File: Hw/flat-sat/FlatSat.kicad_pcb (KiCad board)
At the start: 4 copper layers, 0 parts

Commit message: fet(Hw):Init_floorplan_Update_LCSC#
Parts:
- added C1: 0.1uF, Capacitor_SMD:C_0402_1005Metric, F.Cu at (175.7, 70.3)
- added C10: 1nF, Capacitor_SMD:C_0402_1005Metric, F.Cu at (120.3, 85.0)
- added C11: 470nF, Capacitor_SMD:C_0402_1005Metric, F.Cu at (116.7, 79.4)
- added C12: 1nF, Capacitor_SMD:C_0402_1005Metric, F.Cu at (120.4, 89.4)
- added C13: 0.1uF, Capacitor_SMD:C_0402_1005Metric, F.Cu at (175.7, 80.2)
- added C14: 0.1uF, Capacitor_SMD:C_0402_1005Metric, F.Cu at (178.6, 70.3)
- added C15: 100pF, Capacitor_SMD:C_0402_1005Metric, F.Cu at (161.4, 70.6)
- added C16: 3.3pF, Capacitor_SMD:C_0402_1005Metric, F.Cu at (161.4, 73.1)
- added C17: 3.3pF, Capacitor_SMD:C_0402_1005Metric, F.Cu at (161.4, 75.6)
- added C18: 0.1uF, Capacitor_SMD:C_0402_1005Metric, F.Cu at (178.6, 72.3)
- added C19: 0.1uF, Capacitor_SMD:C_0402_1005Metric, F.Cu at (178.6, 74.3)
- added C2: 100pF, Capacitor_SMD:C_0402_1005Metric, F.Cu at (123.6, 87.2)
- added C20: 47pF, Capacitor_SMD:C_0402_1005Metric, F.Cu at (161.4, 78.1)
- added C21: 1nF, Capacitor_SMD:C_0402_1005Metric, F.Cu at (161.4, 80.6)
- added C22: 470nF, Capacitor_SMD:C_0402_1005Metric, F.Cu at (161.4, 83.2)
- added C23: 1nF, Capacitor_SMD:C_0402_1005Metric, F.Cu at (161.4, 85.7)
- added C24: 0.1uF, Capacitor_SMD:C_0402_1005Metric, F.Cu at (110.8, 81.0)
- added C25: 0.1uF, Capacitor_SMD:C_0402_1005Metric, F.Cu at (109.9, 81.0)
- added C26: 1uF, Capacitor_SMD:C_0402_1005Metric, F.Cu at (111.7, 93.1)
- added C27: 0.1uF, Capacitor_SMD:C_0402_1005Metric, F.Cu at (109.0, 81.0)
- added C28: 0.1uF, Capacitor_SMD:C_0402_1005Metric, F.Cu at (106.2, 81.0)
- added C29: 27pF, Capacitor_SMD:C_0402_1005Metric, F.Cu at (103.6, 94.6)
- added C3: 3.3pF, Capacitor_SMD:C_0402_1005Metric, F.Cu at (125.0, 82.7)
- added C30: 27pF, Capacitor_SMD:C_0402_1005Metric, F.Cu at (108.9, 93.2)
- added C31: 1uF, Capacitor_SMD:C_0402_1005Metric, F.Cu at (114.2, 83.8)
- added C32: 0.1uF, Capacitor_SMD:C_0402_1005Metric, F.Cu at (101.0, 84.6)
- added C33: 0.1uF, Capacitor_SMD:C_0402_1005Metric, F.Cu at (114.2, 84.7)
- added C34: 0.1uF, Capacitor_SMD:C_0402_1005Metric, F.Cu at (114.2, 88.7)
- added C35: 0.1uF, Capacitor_SMD:C_0402_1005Metric, F.Cu at (110.8, 93.1)
- added C36: 0.1uF, Capacitor_SMD:C_0402_1005Metric, F.Cu at (100.8, 88.3)
- added C37: 0.1uF, Capacitor_SMD:C_0402_1005Metric, F.Cu at (184.3, 78.2)
- added C4: 3.3pF, Capacitor_SMD:C_0402_1005Metric, F.Cu at (123.5, 88.7)
- added C5: 0.1uF, Capacitor_SMD:C_0402_1005Metric, F.Cu at (175.7, 72.3)
- added C6: 1uF, Capacitor_SMD:C_0402_1005Metric, F.Cu at (100.2, 72.1)
- added C7: 0.1uF, Capacitor_SMD:C_0402_1005Metric, F.Cu at (94.7, 72.1)
- added C8: 0.1uF, Capacitor_SMD:C_0402_1005Metric, F.Cu at (175.7, 78.2)
- added C9: 47pF, Capacitor_SMD:C_0402_1005Metric, F.Cu at (116.7, 72.2)
- added D1: LED, LED_SMD:LED_0603_1608Metric_Pad1.05x0.95mm_HandSolder, F.Cu at (119.5, 69.8)
- added F1: 0.75A, Fuse:Fuse_0603_1608Metric_Pad1.05x0.95mm_HandSolder, F.Cu at (103.1, 75.3)
- added J1: Antenna, FlatSat:SMA_EDGE, F.Cu at (130.9, 82.5)
- added J2: Antenna, FlatSat:SMA_EDGE, F.Cu at (83.1, 82.5)
- added J3: Serial, Connector_PinHeader_2.54mm:PinHeader_1x04_P2.54mm_Vertical, F.Cu at (164.3, 89.2)
- added J4: SWD, Connector_PinHeader_2.54mm:PinHeader_1x04_P2.54mm_Vertical, F.Cu at (168.9, 89.2)
- added JP1: Jumper, Jumper:SolderJumper-3_P1.3mm_Bridged12_RoundedPad1.0x1.5mm_NumberLabels, F.Cu at (178.5, 92.4)
- added JP2: Jumper, Jumper:SolderJumper-3_P1.3mm_Bridged12_RoundedPad1.0x1.5mm_NumberLabels, F.Cu at (178.5, 95.9)
- added L1: 9.1nH, Inductor_SMD:L_0603_1608Metric, F.Cu at (123.6, 85.8)
- added L2: 47nH, Inductor_SMD:L_0603_1608Metric, F.Cu at (119.6, 72.2)
- added L3: 15uH, Inductor_SMD:L_0603_1608Metric, F.Cu at (118.9, 79.0)
- added L4: 9.1nH, Inductor_SMD:L_0603_1608Metric, F.Cu at (165.4, 78.1)
- added L5: 47nH, Inductor_SMD:L_0603_1608Metric, F.Cu at (165.4, 80.6)
- added L6: 15uH, Inductor_SMD:L_0603_1608Metric, F.Cu at (165.4, 83.2)
- added P1: USB_C_Plug_USB2.0, FlatSat:C393939, F.Cu at (106.8, 72.6)
- added R1: 5k1, Resistor_SMD:R_0402_1005Metric, F.Cu at (110.2, 77.1)
- added R10: 27, Resistor_SMD:R_0402_1005Metric, F.Cu at (108.1, 81.0)
- added R11: 10k, Resistor_SMD:R_0402_1005Metric, F.Cu at (172.8, 76.3)
- added R12: 10k, Resistor_SMD:R_0402_1005Metric, F.Cu at (172.8, 78.3)
- added R13: 1k, Resistor_SMD:R_0402_1005Metric, F.Cu at (109.9, 93.1)
- added R2: 5k1, Resistor_SMD:R_0402_1005Metric, F.Cu at (103.2, 77.1)
- added R3: 100R, Resistor_SMD:R_0402_1005Metric, F.Cu at (169.4, 73.1)
- added R4: 100R, Resistor_SMD:R_0402_1005Metric, F.Cu at (169.4, 75.6)
- added R5: 10k, Resistor_SMD:R_0402_1005Metric, F.Cu at (172.8, 70.3)
- added R6: 100R, Resistor_SMD:R_0402_1005Metric, F.Cu at (169.4, 78.1)
- added R7: 100R, Resistor_SMD:R_0402_1005Metric, F.Cu at (169.4, 80.6)
- added R8: 27, Resistor_SMD:R_0402_1005Metric, F.Cu at (107.1, 81.0)
- added R9: 330, Resistor_SMD:R_0603_1608Metric, F.Cu at (116.3, 69.8)
- added REF**: M2, MountingHole:MountingHole_2.2mm_M2_DIN965_Pad, F.Cu at (85.5, 96.0)
- added REF**: M2, MountingHole:MountingHole_2.2mm_M2_DIN965_Pad, F.Cu at (85.5, 69.0)
- added REF**: M2, MountingHole:MountingHole_2.2mm_M2_DIN965_Pad, F.Cu at (128.5, 69.0)
- added REF**: M2, MountingHole:MountingHole_2.2mm_M2_DIN965_Pad, F.Cu at (128.5, 96.0)
- added U1: TLV75733PDBVR, Package_TO_SOT_SMD:SOT-23-5, F.Cu at (97.5, 72.4)
- added U10: LIS2DH, Package_LGA:LGA-14_2x2mm_P0.35mm_LayoutBorder3x4y, F.Cu at (173.3, 100.1)
- added U2: 0900FM15D0039, FlatSat:0900FM15D0039E, F.Cu at (123.2, 75.9)
- added U3: PE42421, Package_TO_SOT_SMD:SOT-363_SC-70-6, F.Cu at (120.3, 87.2)
- added U4: SX1262IMLTRT, Package_DFN_QFN:QFN-24-1EP_4x4mm_P0.5mm_EP2.65x2.65mm, F.Cu at (119.1, 75.6)
- added U5: W25Q16JV, Package_SON:Winbond_USON-8-2EP_3x4mm_P0.8mm_EP0.2x0.8mm, F.Cu at (102.4, 80.5)
- added U6: 0900FM15D0039, FlatSat:0900FM15D0039E, F.Cu at (123.2, 79.3)
- added U7: PE42421, Package_TO_SOT_SMD:SOT-363_SC-70-6, F.Cu at (173.5, 96.5)
- added U8: SX1262IMLTRT, Package_DFN_QFN:QFN-24-1EP_4x4mm_P0.5mm_EP2.65x2.65mm, F.Cu at (92.5, 79.7)
- added U9: RP2040, Package_DFN_QFN:QFN-56-1EP_7x7mm_P0.4mm_EP3.2x3.2mm, F.Cu at (107.2, 87.3)
- added Y1: 32Mhz, Crystal:Crystal_SMD_2520-4Pin_2.5x2.0mm, F.Cu at (114.2, 75.7)
- added Y2: 32Mhz, Crystal:Crystal_SMD_2520-4Pin_2.5x2.0mm, F.Cu at (97.2, 79.8)
- added Y3: 12MHz, Crystal:Crystal_SMD_3225-4Pin_3.2x2.5mm, F.Cu at (106.4, 94.0)
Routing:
- net Net-(C2-Pad2): track 0.00 -> 3.68 mm
- net Net-(J1-In): track 0.00 -> 3.67 mm
- net Net-(U3-V2): track 0.00 -> 2.23 mm
- net Net-(U3-V1): track 0.00 -> 1.63 mm
- net Net-(U3-RFC): track 0.00 -> 1.59 mm
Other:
- board outline added: 48 x 32 mm

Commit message: feat(Hw):Update_Pcb_And
Pending_some_pins
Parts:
- removed REF** (x4): M2, MountingHole:MountingHole_2.2mm_M2_DIN965_Pad
- added BOOT1: SW, Button_Switch_SMD:SW_SPST_TL3342, F.Cu at (153.0, 18.0)
- added Button1: SW, Button_Switch_SMD:SW_SPST_TL3342, F.Cu at (176.3, 42.4)
- added Button2: SW, Button_Switch_SMD:SW_SPST_TL3342, F.Cu at (187.1, 42.5)
- added RESET1: SW, Button_Switch_SMD:SW_SPST_TL3342, F.Cu at (180.1, 17.4)
- C13, F1, J4, JP1, JP2, R5, U5: moved to B.Cu
- moved C36 91.7 mm to (174.7, 34.0), turned to -45 degrees
- moved C12 89.8 mm to (184.8, 26.8), turned to -90 degrees
- moved C4 89.0 mm to (184.1, 23.6), turned to 90 degrees
- moved C26 87.3 mm to (175.4, 33.4), turned to -45 degrees
- moved L1 86.4 mm to (182.9, 23.0), turned to -90 degrees
- moved C35 86.1 mm to (174.1, 34.7), turned to -45 degrees
- moved U3 86.0 mm to (182.9, 28.3), turned to 90 degrees
- moved R13 85.8 mm to (173.4, 35.4), turned to 135 degrees
- moved C30 85.6 mm to (172.7, 36.1), turned to -45 degrees
- moved C10 85.5 mm to (181.9, 25.7), turned to 90 degrees
- moved Y3 85.5 mm to (170.8, 37.9), turned to 45 degrees
- moved C2 85.5 mm to (182.9, 25.7), turned to 90 degrees
- moved C29 85.4 mm to (169.0, 39.7), turned to 135 degrees
- moved U10 84.8 mm to (189.6, 16.9)
- moved C34 83.6 mm to (167.4, 24.2), turned to 135 degrees
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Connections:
- net Net-(U9-USB_DM) renamed /RD-
- net Net-(U9-USB_DP) renamed /RD+
- J3 pad 2: /RXD -> /TXD
- J3 pad 3: /TXD -> /RXD
- U4 pad 25: unconnected-(U4-EXP-Pad25) -> GND
- U8 pad 25: unconnected-(U8-EXP-Pad25) -> GND
- U9 pad 15: /R1_BUSY -> /Butt_1
- U9 pad 16: /LED1 -> /Butt_2
- U9 pad 17: /Butt_1 -> /R1_BUSY
- U9 pad 18: /Butt_2 -> /LED1
- U9 pad 25: /SWD -> /SWDIO
- U9 pad 36: /R1_CIPO -> /R0_DIO2
- U9 pad 37: /R1_NSS -> /R0_DIO3
- U9 pad 38: /R1_SCK -> /R0_BUSY
- U9 pad 39: /R1_COPI -> /R0_RST
- U9 pad 6: /R0_DIO2 -> /R1_CIPO
- U9 pad 7: /R0_DIO3 -> /R1_NSS
- U9 pad 8: /R0_RST -> /R1_SCK
- U9 pad 9: /R0_BUSY -> /R1_COPI
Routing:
- net +3V3: track 0.00 -> 56.0 mm, vias 0 -> 17
- net GND: track 0.00 -> 50.2 mm, vias 0 -> 15
- net /RESET: track 0.00 -> 39.1 mm, vias 0 -> 2
- net /INT1: track 0.00 -> 38.3 mm, vias 0 -> 3
- net +1V2: track 0.00 -> 36.5 mm, vias 0 -> 2
- net /R1_DIO2: track 0.00 -> 33.3 mm, vias 0 -> 3
- net /QSPI_SS: track 0.00 -> 33.1 mm, vias 0 -> 2
- net /SDA: track 0.00 -> 32.4 mm, vias 0 -> 2
- net /SCL: track 0.00 -> 32.2 mm, vias 0 -> 2
- net /Butt_2: track 0.00 -> 29.0 mm, vias 0 -> 2
- net /TXD: track 0.00 -> 26.0 mm, vias 0 -> 1
- net /RXD: track 0.00 -> 23.2 mm, vias 0 -> 1
- net /R1_ANT_SW: track 0.00 -> 19.9 mm
- net /R0_ANT_SW: track 0.00 -> 18.4 mm, vias 0 -> 2
- net /Butt_1: track 0.00 -> 16.9 mm, vias 0 -> 2
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- added copper zone on F.Cu, net +3V3
- added copper zone on In2.Cu, net +3V3
- added copper zone on B.Cu, net GND
- added copper zone on F.Cu, net GND
- added copper zone on In1.Cu, net GND

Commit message: feat(Hw):Update_Route
Pending_Neo
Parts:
- moved D1 40.8 mm to (186.6, 21.1)
- moved R9 40.8 mm to (183.4, 21.1)
- moved J3 10.6 mm to (158.5, 44.5)
- moved JP1 9.96 mm to (183.1, 34.2)
- moved C4 9.21 mm to (188.1, 31.9), turned to -90 degrees
- moved L1 8.92 mm to (185.8, 31.4)
- moved R4 7.55 mm to (184.1, 33.2), turned to 0 degrees
- moved C12 7.45 mm to (184.1, 34.2), turned to 0 degrees
- moved J4 7.18 mm to (169.8, 44.5)
- moved C3 7.15 mm to (184.1, 30.3), turned to 180 degrees
- moved C2 6.74 mm to (184.1, 32.3), turned to 0 degrees
- moved C10 6.10 mm to (184.1, 31.4), turned to 0 degrees
- moved R3 4.95 mm to (182.3, 30.3), turned to 180 degrees
- moved U3 4.18 mm to (181.6, 32.2), turned to 0 degrees
- moved J2 3.66 mm to (144.5, 26.9)
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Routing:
- net /DIO2: track 1.35 -> 26.8 mm, vias 1 -> 2
- net /R0_DIO2: track 4.99 -> 29.9 mm, vias 0 -> 3
- net /DIO23: track 1.31 -> 23.8 mm, vias 1 -> 2
- net GND: track 50.2 -> 64.1 mm, vias 15 -> 50
- net /TXD: track 26.0 -> 15.3 mm
- net /R1_BUSY: track 0.00 -> 9.49 mm, vias 0 -> 2
- net /RXD: track 23.2 -> 13.9 mm
- net Net-(J1-In): track 15.7 -> 8.27 mm
- net /R1_RST: track 3.05 -> 10.1 mm, vias 1 -> 2
- net /R1_DIO2: track 33.3 -> 39.6 mm
- net /R0_ANT_SW: track 18.4 -> 24.5 mm
- net +1V2: track 36.5 -> 30.5 mm
- net /SWCLK: track 13.0 -> 18.8 mm
- net Net-(J2-In): track 12.1 -> 8.90 mm
- net /SWDIO: track 15.1 -> 18.0 mm
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
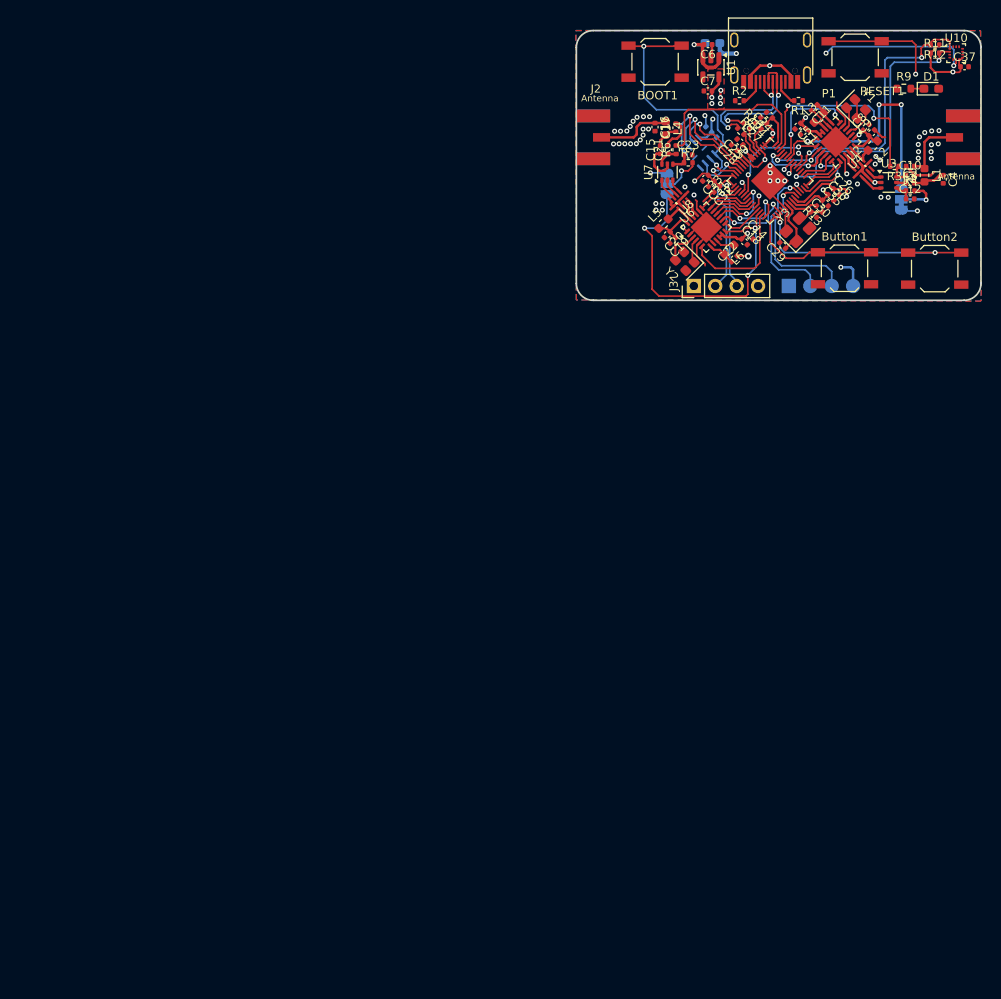
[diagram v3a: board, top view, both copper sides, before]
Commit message: feat(Hw):Mounting_Holes_Added
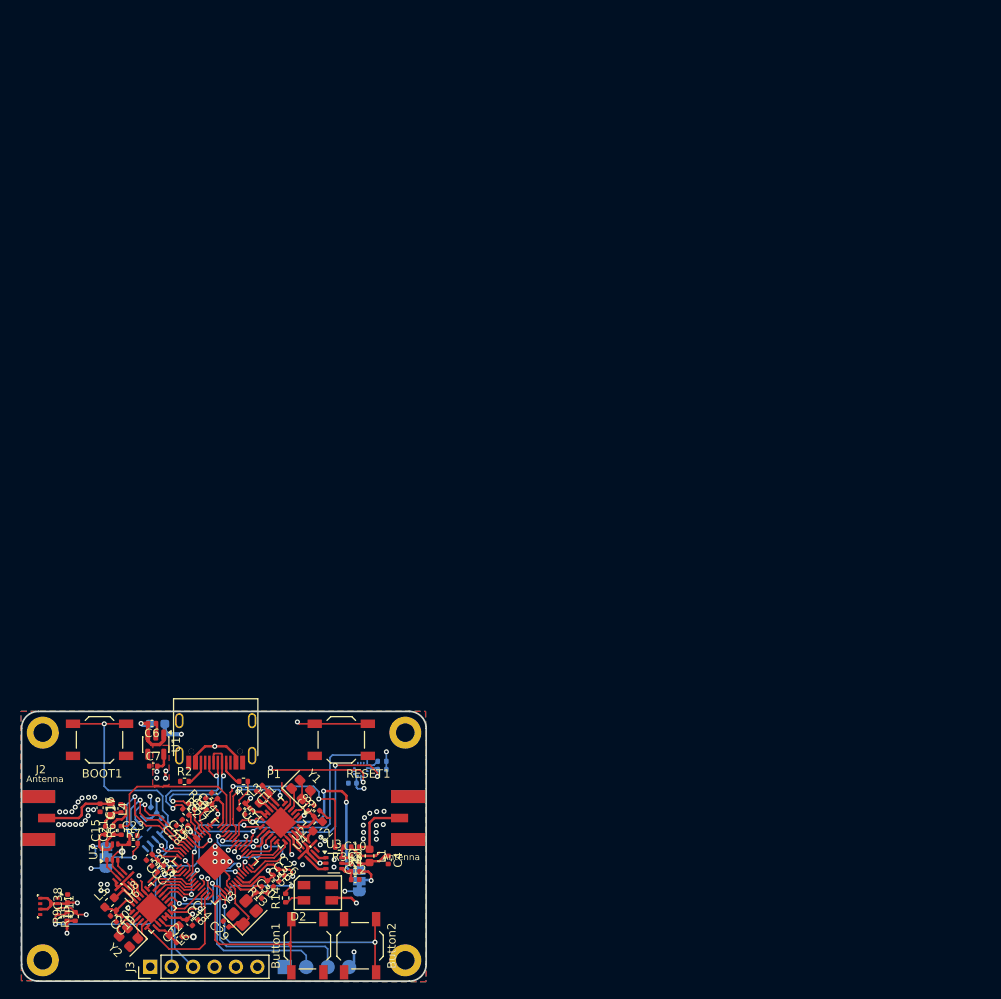
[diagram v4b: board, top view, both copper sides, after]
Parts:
- removed D1: LED, LED_SMD:LED_0603_1608Metric_Pad1.05x0.95mm_HandSolder
- added ?: , , F.Cu at (81.2, 97.5)
- added C38: 0.1uF, Capacitor_SMD:C_0402_1005Metric, F.Cu at (84.2, 117.2)
- added D2: SK6812MINI, Library:SK6812MINI-HS, F.Cu at (113.9, 116.5)
- added R14: 470, Resistor_SMD:R_0402_1005Metric, F.Cu at (110.1, 117.1)
- added R15: 4.7k, Resistor_SMD:R_0402_1005Metric, F.Cu at (85.1, 119.3)
- added REF**: M2, MountingHole:MountingHole_2.2mm_M2_DIN965_Pad, F.Cu at (124.2, 124.5)
- added REF**: M2, MountingHole:MountingHole_2.2mm_M2_DIN965_Pad, F.Cu at (124.2, 97.5)
- added REF**: M2, MountingHole:MountingHole_2.2mm_M2_DIN965_Pad, F.Cu at (81.2, 124.5)
- added U11: BME280 /BMP280, Package_LGA:Bosch_LGA-8_2.5x2.5mm_P0.65mm_ClockwisePinNumbering, F.Cu at (82.0, 118.1)
- C37, R11, R12, U10: moved to B.Cu
- J3: value Serial -> periphs; footprint Connector_PinHeader_2.54mm:PinHeader_1x04_P2.54mm_Vertical -> Connector_PinHeader_2.54mm:PinHeader_1x06_P2.54mm_Vertical
- R9: value 330 -> 4.7k; footprint Resistor_SMD:R_0603_1608Metric -> Resistor_SMD:R_0402_1005Metric
- moved R9 139.6 mm to (84.1, 119.3), turned to 90 degrees
- moved C37 111.8 mm to (118.0, 103.5), turned to 180 degrees
- moved U10 110.5 mm to (119.0, 101.9), turned to 180 degrees
- moved R11 107.4 mm to (121.5, 101.9), turned to 180 degrees
- moved R12 107.4 mm to (121.5, 100.9)
- moved Button2 105.4 mm to (118.9, 122.8), turned to -90 degrees
- moved Y3 104.3 mm to (105.2, 118.8)
- moved C32 104.2 mm to (95.2, 113.7)
- moved C11 104.2 mm to (107.0, 104.1)
- moved C13 104.2 mm to (94.4, 106.7)
- moved C16 104.2 mm to (88.0, 106.4)
- moved C24 104.2 mm to (100.9, 105.6)
- moved C35 104.2 mm to (108.2, 115.4)
- moved C36 104.2 mm to (108.9, 114.8)
- moved F1 104.2 mm to (94.8, 96.5)
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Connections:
- J3 pad 4: +3V3 -> /SCL
- R9 pad 1: GND -> +3V3
- R9 pad 2: Net-(D1-K) -> /SCL
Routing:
- net /SCL: track 32.2 -> 85.9 mm
- net /SDA: track 32.4 -> 73.9 mm, vias 2 -> 4
- net /R1_DIO2: track 39.6 -> 26.0 mm, vias 3 -> 2
- net /LED1: track 0.00 -> 11.1 mm, vias 0 -> 2
- net /INT1: track 38.1 -> 28.4 mm
- net /RESET: track 41.6 -> 31.9 mm
- net /SWDIO: track 18.0 -> 25.4 mm
- net /SWCLK: track 18.8 -> 26.2 mm
- net GND: track 64.1 -> 70.0 mm, vias 50 -> 51
- net +3V3: track 58.1 -> 63.6 mm, vias 18 -> 21
- net /Butt_1: track 16.4 -> 21.6 mm
- net Net-(D2-DIN): track 0.00 -> 2.51 mm
- net Net-(D1-K): track 1.56 -> 0.00 mm
- net Net-(JP1-C): track 5.22 -> 3.74 mm
- net /TXD: track 15.3 -> 14.0 mm
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
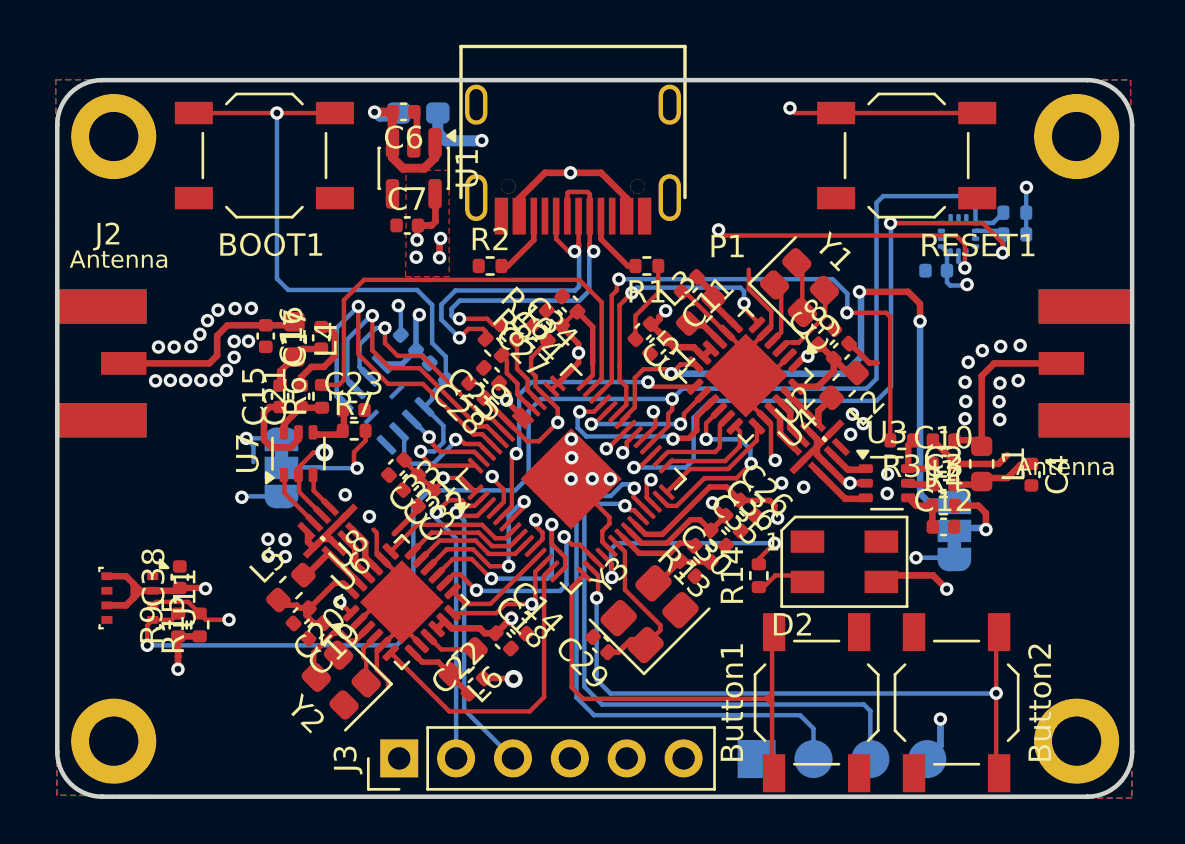
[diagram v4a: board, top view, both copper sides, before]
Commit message: feat(Hw):3D_Model_Added_First_Route
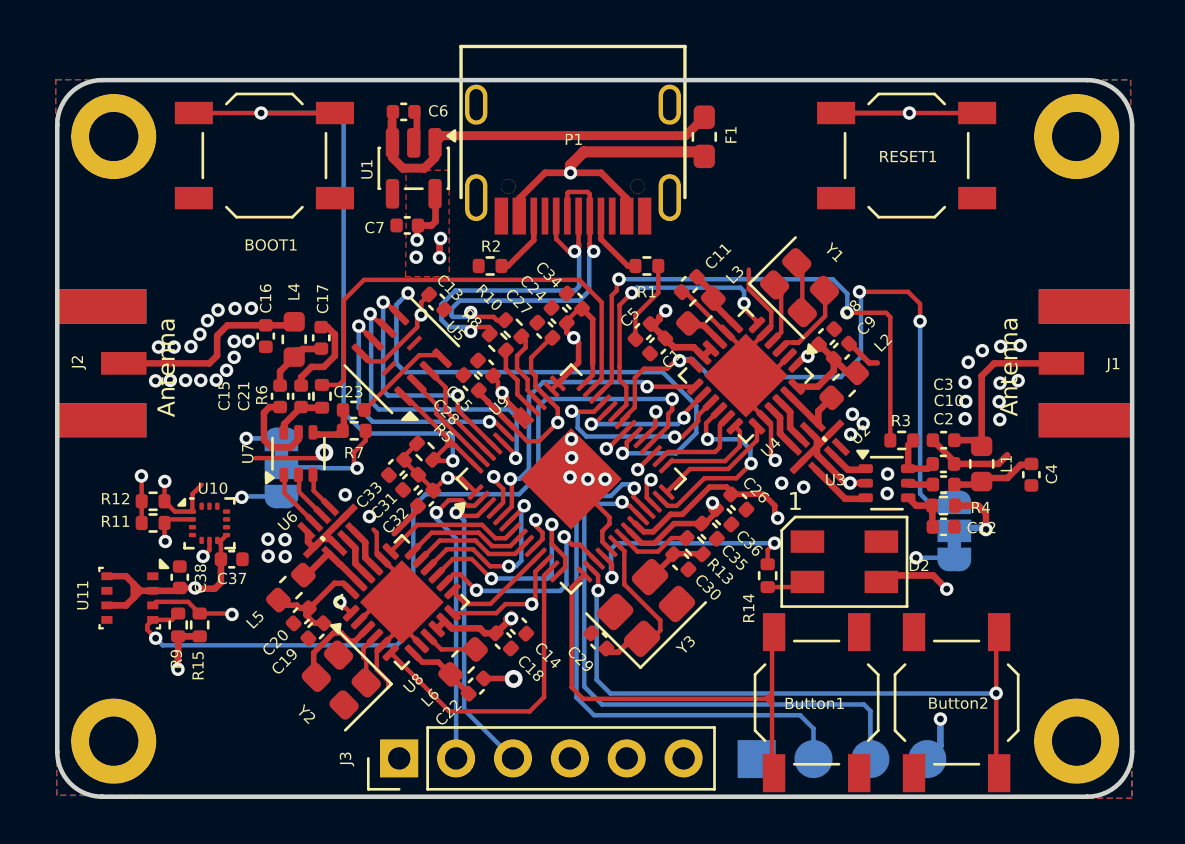
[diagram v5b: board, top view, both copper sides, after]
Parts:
- C13, C37, F1, R11, R12, R5, U10, U5: moved to F.Cu
- moved R11 40.6 mm to (83.0, 114.8), turned to 0 degrees
- moved R12 40.6 mm to (83.0, 113.8), turned to 0 degrees
- moved U10 35.8 mm to (85.5, 114.8), turned to 0 degrees
- moved C37 34.0 mm to (86.5, 116.4), turned to 0 degrees
- moved F1 12.8 mm to (107.6, 97.5), turned to 90 degrees
- moved R5 3.63 mm to (95.2, 111.6)
- moved U5 2.31 mm to (94.1, 107.3)
- moved C13 2.21 mm to (95.7, 104.9), turned to -45 degrees
- moved C36 0.51 mm to (108.5, 114.5)
- moved C35 0.51 mm to (107.8, 115.1)
- moved R13 0.50 mm to (107.2, 115.8)
- moved C26 0.48 mm to (109.2, 113.8)
- moved C30 0.44 mm to (106.6, 116.5)
- moved C28 0.43 mm to (97.2, 108.5)
- moved C25 0.42 mm to (97.8, 107.9)
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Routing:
- net /SDA: track 73.9 -> 54.1 mm, vias 4 -> 3
- net /INT1: track 28.4 -> 46.6 mm
- net /SCL: track 85.9 -> 72.2 mm, vias 2 -> 3
- net VCC: track 7.08 -> 17.1 mm, vias 1 -> 0
- net /RESET: track 31.9 -> 38.3 mm
- net GND: track 70.0 -> 74.7 mm, vias 51 -> 50
- net /QSPI_SS: track 32.7 -> 36.9 mm
- net /QSPI_SD0: track 14.7 -> 11.3 mm, vias 1 -> 2
- net /QSPI_SCK: track 12.9 -> 14.7 mm, vias 1 -> 2
- net Net-(F1-Pad1): track 15.5 -> 14.0 mm, vias 2 -> 1
- net +3V3: track 63.6 -> 64.9 mm, vias 21 -> 20
- net /QSPI_SD2: track 5.86 -> 4.75 mm, vias 1 -> 0
- net /QSPI_SD3: track 10.9 -> 11.7 mm, vias 1 -> 2
- net +1V2: track 30.8 -> 31.5 mm
- net Net-(D2-DIN): track 2.51 -> 1.87 mm
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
